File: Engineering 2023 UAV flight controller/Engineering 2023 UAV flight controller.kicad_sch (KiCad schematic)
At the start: 77 parts, among them J1 Micro_SD_Card, J2 ESC speed control, J3 USB_C_Receptacle_USB2.0, M1 Aileron Left, M2 Aileron Right, M3 Elevator Left, M4 Elevator Right, SW1 SW_SPDT, SW2 4FSH922, U1 W25Q128JVS, U2 AMS1117-3.3, U3 LM350_TO220, U4 RP2040, U5 LPS25HB, U6 MPU-6050, U7 MMC5983MA, U8 E28-2G4M27S, U9 NEO-M8N, Y1 ABLS-12.000MHZ-B4-T

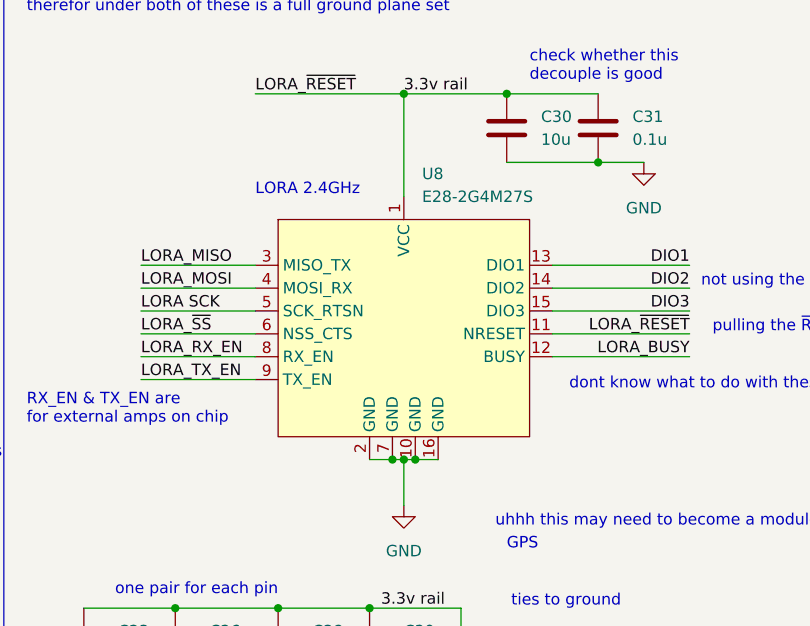
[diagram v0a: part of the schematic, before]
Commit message: finaly merged the change i wanted, the lora module now has a footprint
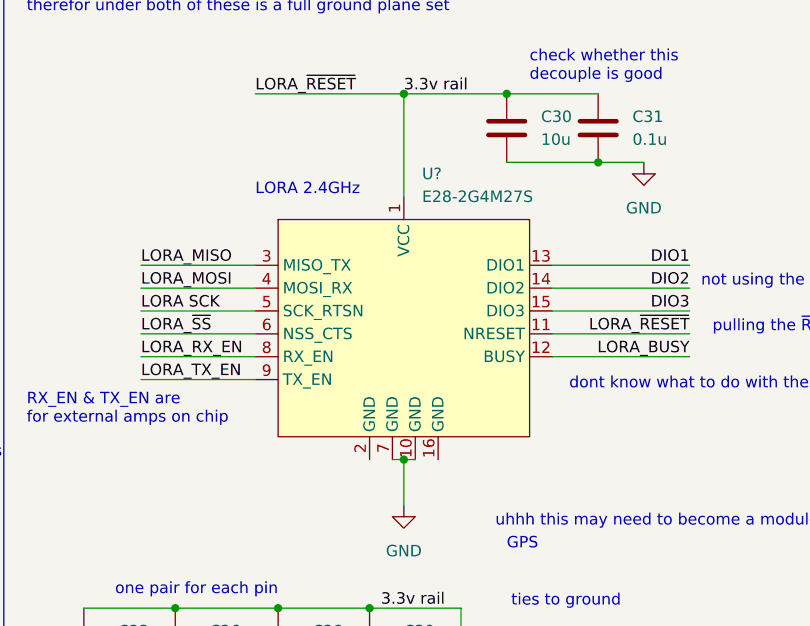
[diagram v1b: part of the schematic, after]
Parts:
- removed U8: E28-2G4M27S, symbol SX1280:E28-2G4M27S
- added U?: E28-2G4M27S, SX1280:E28-2G4M27S, symbol SX1280:E28-2G4M27S
- J?: footprint (none) -> Connector_DIN:DIN41612_B2_2x16_Female_Vertical_THT
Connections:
- net 3.3v rail: now also U?.1 (VCC), U?.11 (NRESET)
- net DIO1: now also U?.13 (DIO1)
- net DIO2: now also U?.14 (DIO2)
- net DIO3: now also U?.15 (DIO3)
- net GND: now also U?.10 (GND), U?.7 (GND)
- net LORA SCK: now also U?.5 (SCK_RTSN)
- net LORA_BUSY: now also U?.12 (BUSY)
- net LORA_MISO: now also U?.3 (MISO_TX)
- net LORA_MOSI: now also U?.4 (MOSI_RX)
- net LORA_RX_EN: now also U?.8 (RX_EN)
- net LORA_TX_EN: now also U?.9 (TX_EN)
- net LORA_~{SS}: now also U?.6 (NSS_CTS)
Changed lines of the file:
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@@
   (junction (at 245.11 217.17) (diameter 0) (color 0 0 0 0)
   )
-  (junction (at 252.73 193.04) (diameter 0) (color 0 0 0 0)
-  )
   (junction (at 379.73 110.49) (diameter 0) (color 0 0 0 0)
   )
@@
   (junction (at 283.21 36.83) (diameter 0) (color 0 0 0 0)
   )
-  (junction (at 255.27 193.04) (diameter 0) (color 0 0 0 0)
-  )
   (no_connect (at 247.65 255.27))
   (no_connect (at 379.73 119.38))
@@
     (stroke (width 0) (type default) (color 0 0 0 0))
   )
-  (wire (pts (xy 255.27 193.04) (xy 257.81 193.04))
+  (wire (pts (xy 254 193.04) (xy 255.27 193.04))
     (stroke (width 0) (type default) (color 0 0 0 0))
   )
@@
     (stroke (width 0) (type default) (color 0 0 0 0))
   )
-  (wire (pts (xy 250.19 193.04) (xy 252.73 193.04))
+  (wire (pts (xy 250.19 193.04) (xy 250.19 193.04))
     (stroke (width 0) (type default) (color 0 0 0 0))
   )
@@
     (stroke (width 0) (type default) (color 0 0 0 0))
   )
-  (wire (pts (xy 254 193.04) (xy 255.27 193.04))
-    (stroke (width 0) (type default) (color 0 0 0 0))
-  )
   (wire (pts (xy 224.79 102.87) (xy 227.33 102.87))
     (stroke (width 0) (type default) (color 0 0 0 0))
@@
     (stroke (width 0) (type default) (color 0 0 0 0))
   )
-  (wire (pts (xy 252.73 193.04) (xy 254 193.04))
-    (stroke (width 0) (type default) (color 0 0 0 0))
-  )
   (wire (pts (xy 379.73 105.41) (xy 379.73 106.68))
     (stroke (width 0) (type default) (color 0 0 0 0))
@@
     (stroke (width 0) (type default) (color 0 0 0 0))
   )
+  (wire (pts (xy 257.81 193.04) (xy 257.81 193.04))
+    (stroke (width 0) (type default) (color 0 0 0 0))
+  )
   (wire (pts (xy 224.79 86.36) (xy 256.54 86.36))
     (stroke (width 0) (type default) (color 0 0 0 0))
@@
     (stroke (width 0) (type default) (color 0 0 0 0))
   )
+  (wire (pts (xy 252.73 193.04) (xy 254 193.04))
+    (stroke (width 0) (type default) (color 0 0 0 0))
+  )
   (wire (pts (xy 368.3 25.4) (xy 388.62 25.4))
     (stroke (width 0) (type default) (color 0 0 0 0))
@@
     (pin "2")
   )
-  (symbol (lib_id "SX1280:E28-2G4M27S") (at 217.17 143.51 0) (unit 1)
-    (in_bom yes) (on_board yes) (fields_autoplaced)
-    (property "Reference" "U8" (id 0) (at 256.0194 161.29 0)
-      (effects (font (size 1.27 1.27)) (justify left))
-    )
-    (property "Value" "E28-2G4M27S" (id 1) (at 256.0194 163.83 0)
-      (effects (font (size 1.27 1.27)) (justify left))
-    )
-    (property "Footprint" "" (id 2) (at 217.17 143.51 0)
-      (effects (font (size 1.27 1.27)) hide)
-    )
-    (property "Datasheet" "" (id 3) (at 217.17 143.51 0)
-      (effects (font (size 1.27 1.27)) hide)
-    )
-    (pin "1")
-    (pin "10")
-    (pin "11")
-    (pin "12")
-    (pin "13")
-    (pin "14")
-    (pin "15")
-    (pin "16")
-    (pin "2")
-    (pin "3")
-    (pin "4")
-    (pin "5")
-    (pin "6")
-    (pin "7")
-    (pin "8")
-    (pin "9")
-  )
   (symbol (lib_id "power:GND") (at 368.3 73.66 0) (unit 1)
     (in_bom yes) (on_board yes) (fields_autoplaced)
@@
     (pin "2")
   )
+  (symbol (lib_id "SX1280:E28-2G4M27S") (at 238.76 165.1 0) (unit 1)
+    (in_bom yes) (on_board yes) (fields_autoplaced)
+    (property "Reference" "U?" (id 0) (at 256.0194 161.29 0)
+      (effects (font (size 1.27 1.27)) (justify left))
+    )
+    (property "Value" "E28-2G4M27S" (id 1) (at 256.0194 163.83 0)
+      (effects (font (size 1.27 1.27)) (justify left))
+    )
+    (property "Footprint" "SX1280:E28-2G4M27S" (id 2) (at 271.78 195.58 0)
+      (effects (font (size 1.27 1.27)) hide)
+    )
+    (property "Datasheet" "https://www.ebyte.com/en/downpdf.aspx?id=537" (id 3) (at 284.48 193.04 0)
+      (effects (font (size 1.27 1.27)) hide)
+    )
+    (pin "1")
+    (pin "10")
+    (pin "11")
+    (pin "12")
+    (pin "13")
+    (pin "14")
+    (pin "15")
+    (pin "16")
+    (pin "2")
+    (pin "3")
+    (pin "4")
+    (pin "5")
+    (pin "6")
+    (pin "7")
+    (pin "8")
+    (pin "9")
+  )
   (symbol (lib_id "Switch:SW_SPDT") (at 49.53 26.67 0) (mirror y) (unit 1)
     (in_bom yes) (on_board yes) (fields_autoplaced)
@@
     (property "Reference" "J?" (id 0) (at 375.92 172.72 0))
     (property "Value" "external power rails" (id 1) (at 375.92 175.26 0))
-    (property "Footprint" "" (id 2) (at 374.65 189.23 0)
+    (property "Footprint" "Connector_DIN:DIN41612_B2_2x16_Female_Vertical_THT" (id 2) (at 374.65 189.23 0)
       (effects (font (size 1.27 1.27)) hide)
     )
@@
       (reference "U7") (unit 1) (value "MMC5983MA") (footprint "MMC5983MA_MEM")
     )
-    (path "/2fad4847-f932-40e7-a067-d76f37f4cf43"
-      (reference "U8") (unit 1) (value "E28-2G4M27S") (footprint "")
-    )
     (path "/e13b45e6-ba83-4cc9-8b4d-4ff4bcc84adc"
       (reference "U9") (unit 1) (value "NEO-M8N") (footprint "RF_GPS:ublox_NEO")
     )
+    (path "/48e6ae9c-2b96-4b89-bc19-8b5e9d4f9e9b"
+      (reference "U?") (unit 1) (value "E28-2G4M27S") (footprint "SX1280:E28-2G4M27S")
+    )
     (path "/0261b40d-5a8c-4d5c-ac37-e46612ace541"

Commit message: finished schematic
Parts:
- removed AE1: APAE1575R1540AZDB2F-T, symbol Device:Antenna
- removed J?: External pinout, symbol Connector_Generic:Conn_01x10
- added C35: 47p, Capacitor_SMD:C_0603_1608Metric, symbol Device:C
- added J4: Conn_Coaxial, Connector_Coaxial:SMA_Amphenol_901-143_Horizontal, symbol Connector:Conn_Coaxial
- added J6: Board GPIO and the Lora DIO, Connector_PinSocket_2.54mm:PinSocket_1x13_P2.54mm_Vertical, symbol Connector_Generic:Conn_01x13
- added L1: 27n, Inductor_SMD:L_0603_1608Metric, symbol Device:L
- added R17: 10, Resistor_SMD:R_0603_1608Metric, symbol Device:R
- added SW3: SW_Push, Button_Switch_SMD:SW_SPST_Omron_B3FS-100xP, symbol Switch:SW_Push
- C1, C10, C11, C12, C13, C14, C15, C16, C17, C18, C19, C2, C20, C21, C22, C23, C24, C25, C26, C27, C28, C29, C3, C30, C31, C32, C33, C34, C4, C5, C6, C7, C8, C9: footprint (none) -> Capacitor_SMD:C_0603_1608Metric
- D1, D2, D3, D4: footprint (none) -> LED_SMD:LED_0603_1608Metric
- J1: footprint (none) -> Connector_Card:microSD_HC_Hirose_DM3AT-SF-PEJM5
- J2, M1, M2, M3, M4: footprint (none) -> Connector_PinSocket_2.54mm:PinSocket_1x03_P2.54mm_Vertical
- JP1: footprint (none) -> Jumper:SolderJumper-2_P1.3mm_Bridged_RoundedPad1.0x1.5mm
- R1, R10, R11, R12, R13, R14, R15, R16, R2, R3, R4, R5, R6, R7, R8, R9: footprint (none) -> Resistor_SMD:R_0603_1608Metric
- SW1: footprint (none) -> Button_Switch_SMD:SW_SPDT_CK-JS102011SAQN
- SW2: footprint (none) -> Button_Switch_SMD:SW_MEC_5GSH9
- Y1: footprint (none) -> Crystal:Crystal_SMD_HC49-SD
- gave numbers to parts that had none: 2
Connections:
- net 3.3v rail: no longer U8.11 (NRESET)
- net DIO1: now also J6.11 (Pin_11)
- net DIO2: now also J6.12 (Pin_12)
- net DIO3: now also J6.13 (Pin_13)
- net External_pin_1: now also J6.1 (Pin_1)
- net External_pin_10: now also J6.10 (Pin_10)
- net External_pin_2: now also J6.2 (Pin_2)
- net External_pin_3: now also J6.3 (Pin_3)
- net External_pin_4: now also J6.4 (Pin_4)
- net External_pin_5: now also J6.5 (Pin_5)
- net External_pin_6: now also J6.6 (Pin_6)
- net External_pin_7: now also J6.7 (Pin_7)
- net External_pin_8: now also J6.8 (Pin_8)
- net External_pin_9: now also J6.9 (Pin_9)
- net GND: now also C35.2, J4.2 (Ext), SW3.2
- net NEO_RF_IN: now also J4.1 (In), L1.2
- net NEO_VCC_RF: now also R17.1
- net NEO_LNA_EN: no longer names the net of U9.14 (LNA_EN)
- new net: C35.1, L1.1, R17.2
- new net LORA_~{RESET}: SW3.1, U8.11 (NRESET)
- no-connect marks 12 -> 13
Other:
- note added: "dont ask, I dont know, google says phantom power"
- note added: "pin out DIO incase want to connect to rp2040"
- note added: "pins 13 to 22 on rp2040 DIO 1-3 on lora"
- note added: "these two are a guess from app note"
- note removed: "need to decide on rf ant stuff before pcb can be designed"
- note removed: "not using the DIO"
- note removed: "pins 13 to 22 on rp2040"
- note removed: "pulling the ~{RESET} high to prevent it reseting"
- moved on the sheet: J5

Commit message: finished schematic
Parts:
- removed J5: external power rails, Connector_DIN:DIN41612_B2_2x16_Female_Vertical_THT, symbol Connector_Generic:Conn_02x10_Top_Bottom
- removed U2: AMS1117-3.3, Package_TO_SOT_SMD:SOT-223-3_TabPin2, symbol Regulator_Linear:AMS1117-3.3
- added J5: external power rail, Connector_PinHeader_2.54mm:PinHeader_1x10_P2.54mm_Vertical, symbol Connector_Generic:Conn_01x10
- added J7: external ground rail, Connector_PinHeader_2.54mm:PinHeader_1x10_P2.54mm_Vertical, symbol Connector_Generic:Conn_01x10
- added U2: NCP1117-3.3_TO252, Package_TO_SOT_SMD:TO-252-2, symbol Regulator_Linear:NCP1117-3.3_TO252
- U7: footprint MMC5983MA_MEM -> MMC5983MA:MMC5983MA
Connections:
- net 3.3v rail: now also J5.1 (Pin_1), J5.10 (Pin_10), J5.2 (Pin_2), J5.3 (Pin_3), J5.4 (Pin_4), J5.5 (Pin_5), J5.6 (Pin_6), J5.7 (Pin_7), J5.8 (Pin_8), J5.9 (Pin_9), U2.2 (VO)
- net GND: now also U8.16 (GND), U8.2 (GND), J7.1 (Pin_1), J7.10 (Pin_10), J7.2 (Pin_2), J7.3 (Pin_3), J7.4 (Pin_4), J7.5 (Pin_5), J7.6 (Pin_6), J7.7 (Pin_7), J7.8 (Pin_8), J7.9 (Pin_9), U2.1 (GND)
- net reg in: now also U2.3 (VI)

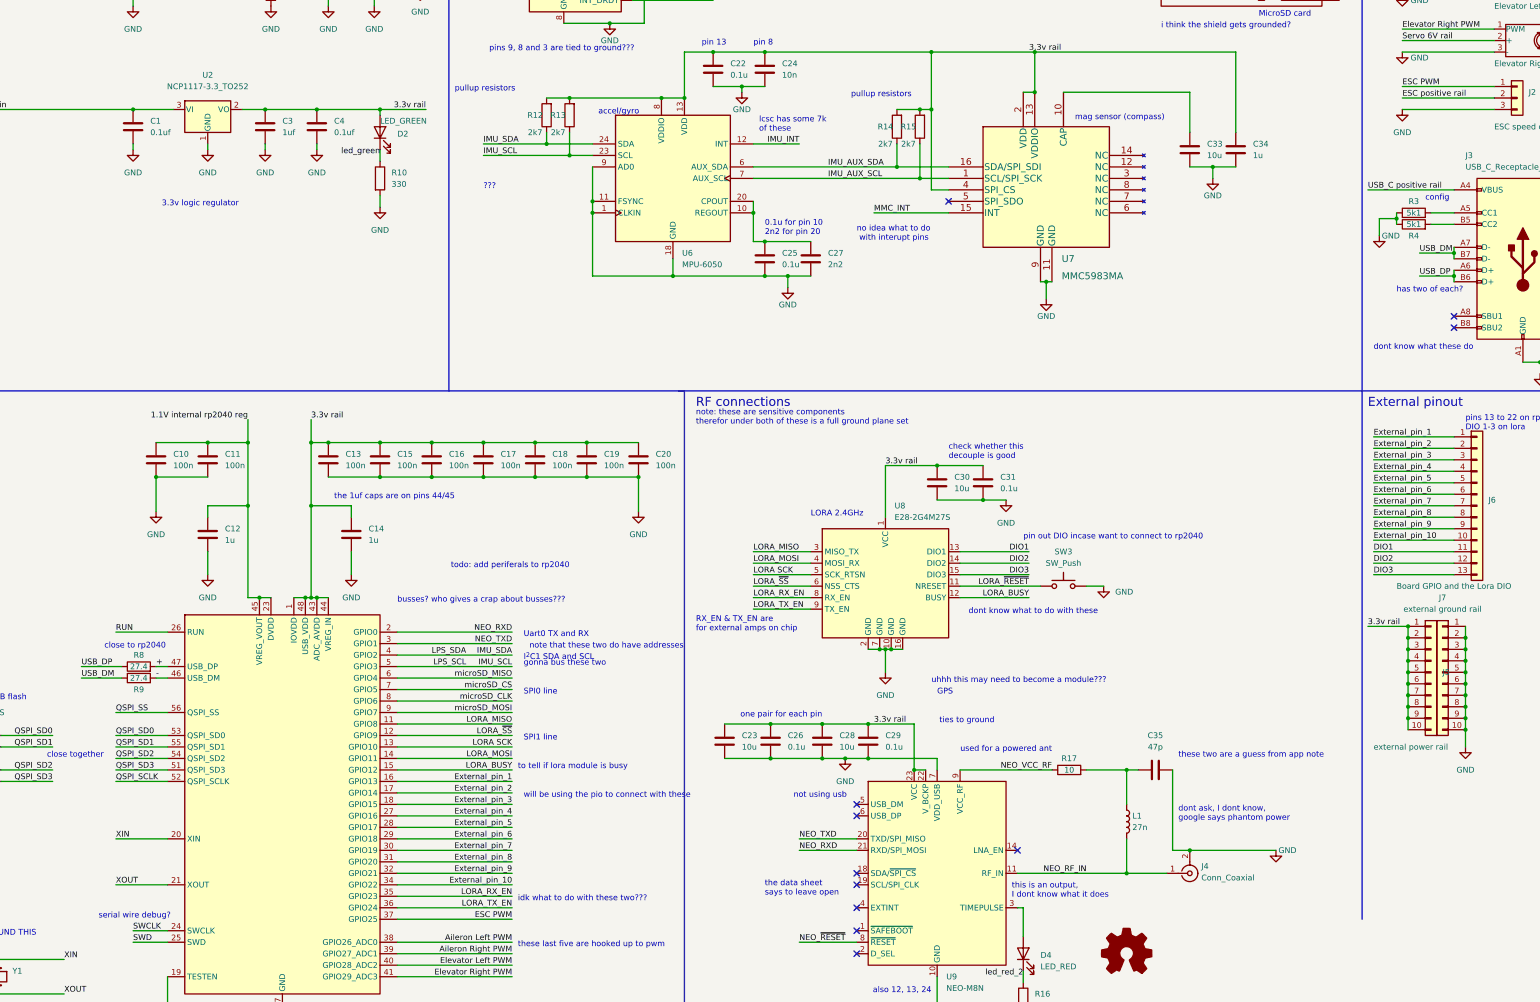
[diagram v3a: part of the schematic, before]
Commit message: fixed some 3d shapes
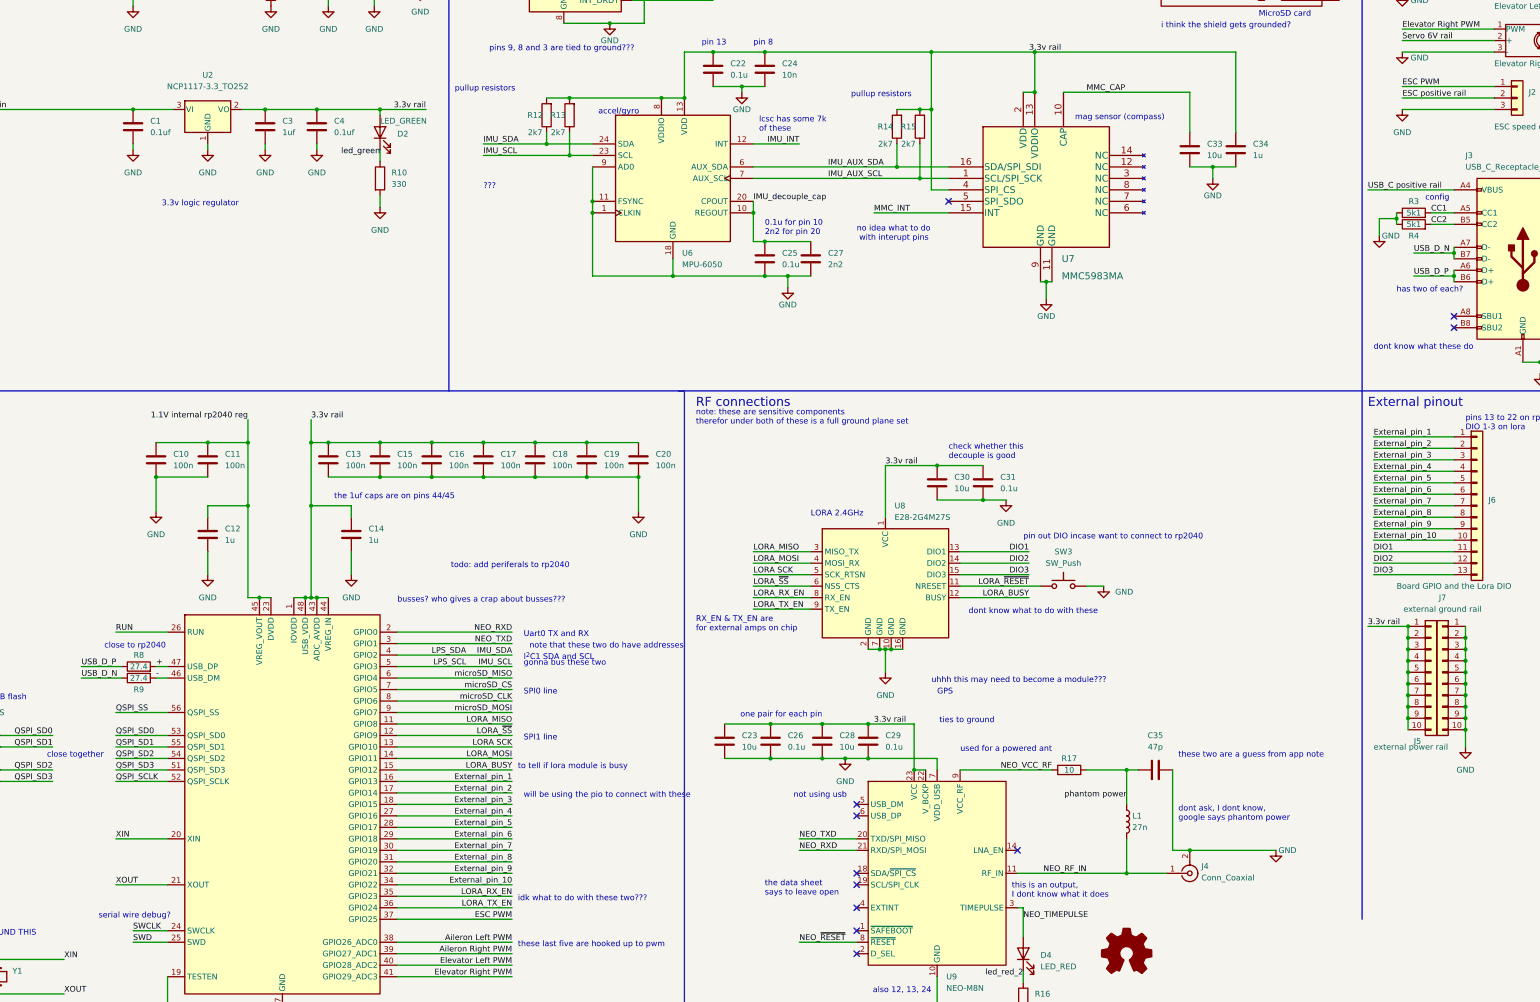
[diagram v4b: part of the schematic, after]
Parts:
- J1: footprint Connector_Card:microSD_HC_Hirose_DM3AT-SF-PEJM5 -> Connector_Card:microSD_HC_Hirose_DM3D-SF
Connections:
- net CC1: now reaches J3.A5 (CC1), R3.2
- net MMC_CAP: now reaches C33.2, U7.10 (CAP)
- net phantom power: now reaches C35.1, L1.1, R17.2
- net CC2: now reaches J3.B5 (CC2), R4.2
- net IMU_decouple_cap: now reaches C25.2, C27.2, U6.10 (REGOUT), U6.20 (CPOUT)
- net NEO_TIMEPULSE: now reaches D4.2 (A), U9.3 (TIMEPULSE)
- net USB_DM renamed USB_D_N
- net USB_DP renamed USB_D_P
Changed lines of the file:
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@@
     (stroke (width 0) (type default) (color 0 0 0 0))
   )
-  (wire (pts (xy 372.11 110.49) (xy 379.73 110.49))
+  (wire (pts (xy 370.84 110.49) (xy 379.73 110.49))
     (stroke (width 0) (type default) (color 0 0 0 0))
   )
@@
     (stroke (width 0) (type default) (color 0 0 0 0))
   )
-  (wire (pts (xy 372.11 105.41) (xy 379.73 105.41))
+  (wire (pts (xy 370.84 105.41) (xy 379.73 105.41))
     (stroke (width 0) (type default) (color 0 0 0 0))
   )
@@
     (effects (font (size 1.27 1.27)) (justify left bottom))
   )
+  (label "CC1" (at 374.65 96.52 0)
+    (effects (font (size 1.27 1.27)) (justify left bottom))
+  )
   (label "SWD" (at 87.63 257.81 0)
     (effects (font (size 1.27 1.27)) (justify left bottom))
@@
     (effects (font (size 1.27 1.27)) (justify left bottom))
   )
+  (label "IMU_decouple_cap" (at 224.79 93.98 0)
+    (effects (font (size 1.27 1.27)) (justify left bottom))
+  )
   (label "Aileron Left PWM" (at 368.3 20.32 0)
     (effects (font (size 1.27 1.27)) (justify left bottom))
@@
     (effects (font (size 1.27 1.27)) (justify right bottom))
   )
+  (label "NEO_TIMEPULSE" (at 284.48 252.73 0)
+    (effects (font (size 1.27 1.27)) (justify left bottom))
+  )
   (label "External_pin_9" (at 171.45 242.57 180)
     (effects (font (size 1.27 1.27)) (justify right bottom))
@@
     (effects (font (size 1.27 1.27)) (justify left bottom))
   )
+  (label "phantom power" (at 307.34 226.06 180)
+    (effects (font (size 1.27 1.27)) (justify right bottom))
+  )
   (label "QSPI_SD1" (at 83.82 214.63 0)
     (effects (font (size 1.27 1.27)) (justify left bottom))
@@
     (effects (font (size 1.27 1.27)) (justify left bottom))
   )
-  (label "USB_DP" (at 372.11 110.49 0)
+  (label "CC2" (at 374.65 99.06 0)
+    (effects (font (size 1.27 1.27)) (justify left bottom))
+  )
+  (label "USB_D_P" (at 370.84 110.49 0)
     (effects (font (size 1.27 1.27)) (justify left bottom))
   )
@@
     (effects (font (size 1.27 1.27)) (justify right bottom))
   )
-  (label "USB_DM" (at 76.2 199.39 0)
+  (label "USB_D_N" (at 76.2 199.39 0)
     (effects (font (size 1.27 1.27)) (justify left bottom))
   )
@@
     (effects (font (size 1.27 1.27)) (justify left bottom))
   )
+  (label "MMC_CAP" (at 298.45 69.85 0)
+    (effects (font (size 1.27 1.27)) (justify left bottom))
+  )
   (label "led_green" (at 142.24 83.82 180)
     (effects (font (size 1.27 1.27)) (justify right bottom))
@@
     (effects (font (size 1.27 1.27)) (justify right bottom))
   )
-  (label "USB_DM" (at 372.11 105.41 0)
+  (label "USB_D_N" (at 370.84 105.41 0)
     (effects (font (size 1.27 1.27)) (justify left bottom))
   )
-  (label "USB_DP" (at 76.2 196.85 0)
+  (label "USB_D_P" (at 76.2 196.85 0)
     (effects (font (size 1.27 1.27)) (justify left bottom))
   )
@@
   (symbol (lib_id "Connector_Generic:Conn_01x10") (at 374.65 198.12 0) (unit 1)
     (in_bom yes) (on_board yes)
-    (property "Reference" "J5" (id 0) (at 377.19 198.1199 0)
+    (property "Reference" "J5" (id 0) (at 370.84 213.36 0)
       (effects (font (size 1.27 1.27)) (justify left))
     )
@@
     (property "Reference" "J1" (id 0) (at 334.645 15.24 0))
     (property "Value" "Micro_SD_Card" (id 1) (at 334.645 17.78 0))
-    (property "Footprint" "Connector_Card:microSD_HC_Hirose_DM3AT-SF-PEJM5" (id 2) (at 363.22 44.45 0)
+    (property "Footprint" "Connector_Card:microSD_HC_Hirose_DM3D-SF" (id 2) (at 363.22 44.45 0)
       (effects (font (size 1.27 1.27)) hide)
     )
@@
     )
     (path "/b831070f-41fa-4fff-9268-47aed16ea16b"
-      (reference "J1") (unit 1) (value "Micro_SD_Card") (footprint "Connector_Card:microSD_HC_Hirose_DM3AT-SF-PEJM5")
+      (reference "J1") (unit 1) (value "Micro_SD_Card") (footprint "Connector_Card:microSD_HC_Hirose_DM3D-SF")
     )
     (path "/ee2d7551-8ac1-4618-9348-753907aeb052"
